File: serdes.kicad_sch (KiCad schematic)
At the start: 11 parts, among them U1 LFE5U-85F-6BG381C

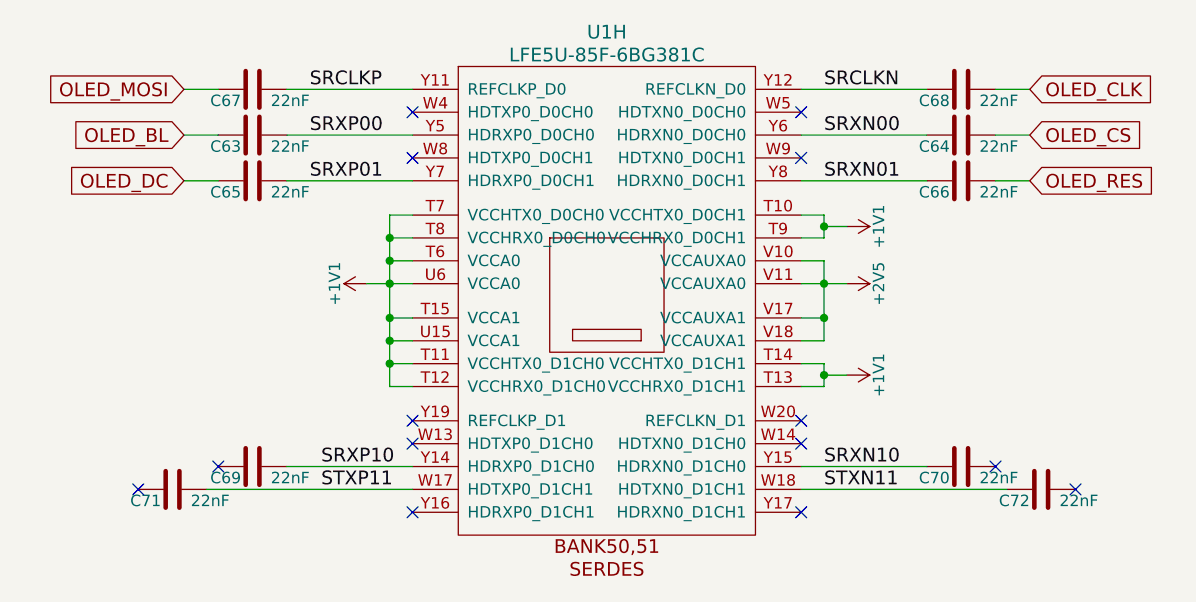
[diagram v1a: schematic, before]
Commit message: remove a few more oled things
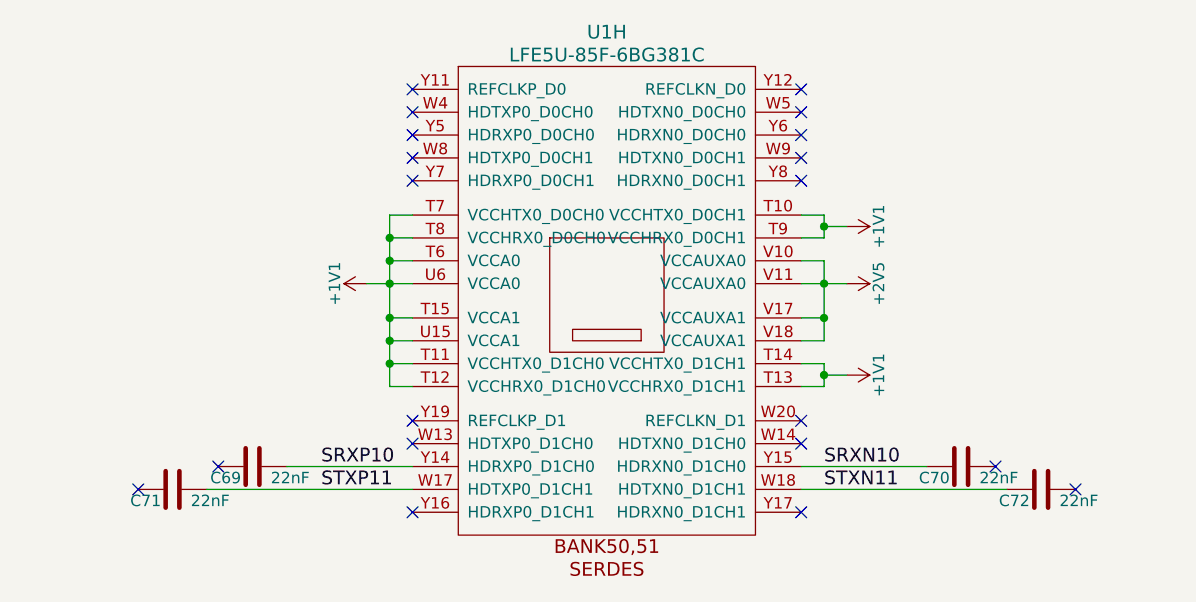
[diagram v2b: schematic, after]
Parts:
- removed C63, C64, C65, C66, C67, C68: 22nF, Capacitor_SMD:C_0603_1608Metric, symbol Device:C
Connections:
- net SRCLKN: no longer names the net of U1.Y12 (REFCLKN_D0)
- net SRCLKP: no longer names the net of U1.Y11 (REFCLKP_D0)
- net SRXN00: no longer names the net of U1.Y6 (HDRXN0_D0CH0)
- net SRXN01: no longer names the net of U1.Y8 (HDRXN0_D0CH1)
- net SRXP00: no longer names the net of U1.Y5 (HDRXP0_D0CH0)
- net SRXP01: no longer names the net of U1.Y7 (HDRXP0_D0CH1)
- no-connect marks 14 -> 20

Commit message: start to normalize bom
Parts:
- C69, C70, C71, C72: Digikey (none) -> 587-1238-1-ND; LCSC (none) -> C107137; MPN (none) -> CX0603MRX7R8BB223
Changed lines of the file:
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@@
+			)
+		)
+		(property "LCSC" "C107137"
+			(at 184.15 91.44 90)
+			(effects
+				(font
+					(size 1.27 1.27)
+				)
+				(hide yes)
+			)
+		)
+		(property "Digikey" "587-1238-1-ND"
+			(at 184.15 91.44 90)
+			(effects
+				(font
+					(size 1.27 1.27)
+				)
+				(hide yes)
+			)
+		)
+		(property "MPN" "CX0603MRX7R8BB223"
+			(at 184.15 91.44 90)
+			(effects
+				(font
+					(size 1.27 1.27)
+				)
+				(hide yes)
 			)
 		)
@@
 			)
 		)
+		(property "LCSC" "C107137"
+			(at 105.41 91.44 90)
+			(effects
+				(font
+					(size 1.27 1.27)
+				)
+				(hide yes)
+			)
+		)
+		(property "Digikey" "587-1238-1-ND"
+			(at 105.41 91.44 90)
+			(effects
+				(font
+					(size 1.27 1.27)
+				)
+				(hide yes)
+			)
+		)
+		(property "MPN" "CX0603MRX7R8BB223"
+			(at 105.41 91.44 90)
+			(effects
+				(font
+					(size 1.27 1.27)
+				)
+				(hide yes)
+			)
+		)
 		(pin "1"
 		)
@@
 			)
 		)
+		(property "LCSC" "C107137"
+			(at 96.52 93.98 90)
+			(effects
+				(font
+					(size 1.27 1.27)
+				)
+				(hide yes)
+			)
+		)
+		(property "Digikey" "587-1238-1-ND"
+			(at 96.52 93.98 90)
+			(effects
+				(font
+					(size 1.27 1.27)
+				)
+				(hide yes)
+			)
+		)
+		(property "MPN" "CX0603MRX7R8BB223"
+			(at 96.52 93.98 90)
+			(effects
+				(font
+					(size 1.27 1.27)
+				)
+				(hide yes)
+			)
+		)
 		(pin "1"
 		)
@@
 			)
 		)
+		(property "LCSC" "C107137"
+			(at 193.04 93.98 90)
+			(effects
+				(font
+					(size 1.27 1.27)
+				)
+				(hide yes)
+			)
+		)
+		(property "Digikey" "587-1238-1-ND"
+			(at 193.04 93.98 90)
+			(effects
+				(font
+					(size 1.27 1.27)
+				)
+				(hide yes)
+			)
+		)
+		(property "MPN" "CX0603MRX7R8BB223"
+			(at 193.04 93.98 90)
+			(effects
+				(font
+					(size 1.27 1.27)
+				)
+				(hide yes)
+			)
+		)

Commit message: updating part numbers across schematcs
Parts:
- C69, C70, C71, C72: MPN CX0603MRX7R8BB223 -> CC0603JRX7R8BB223
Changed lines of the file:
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@@
 			)
 		)
-		(property "MPN" "CX0603MRX7R8BB223"
+		(property "MPN" "CC0603JRX7R8BB223"
 			(at 184.15 91.44 90)
 			(effects
@@
 			)
 		)
-		(property "MPN" "CX0603MRX7R8BB223"
+		(property "MPN" "CC0603JRX7R8BB223"
 			(at 105.41 91.44 90)
 			(effects
@@
 			)
 		)
-		(property "MPN" "CX0603MRX7R8BB223"
+		(property "MPN" "CC0603JRX7R8BB223"
 			(at 96.52 93.98 90)
 			(effects
@@
 			)
 		)
-		(property "MPN" "CX0603MRX7R8BB223"
+		(property "MPN" "CC0603JRX7R8BB223"
 			(at 193.04 93.98 90)
 			(effects

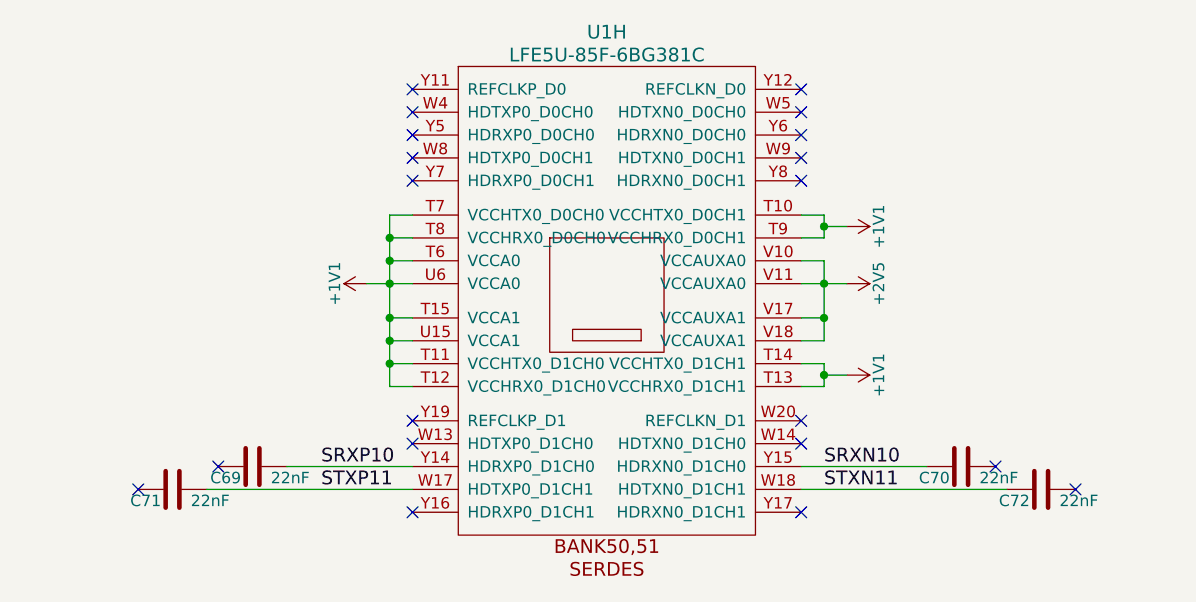
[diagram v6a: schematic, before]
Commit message: remove serdes. fix led connectivity issues
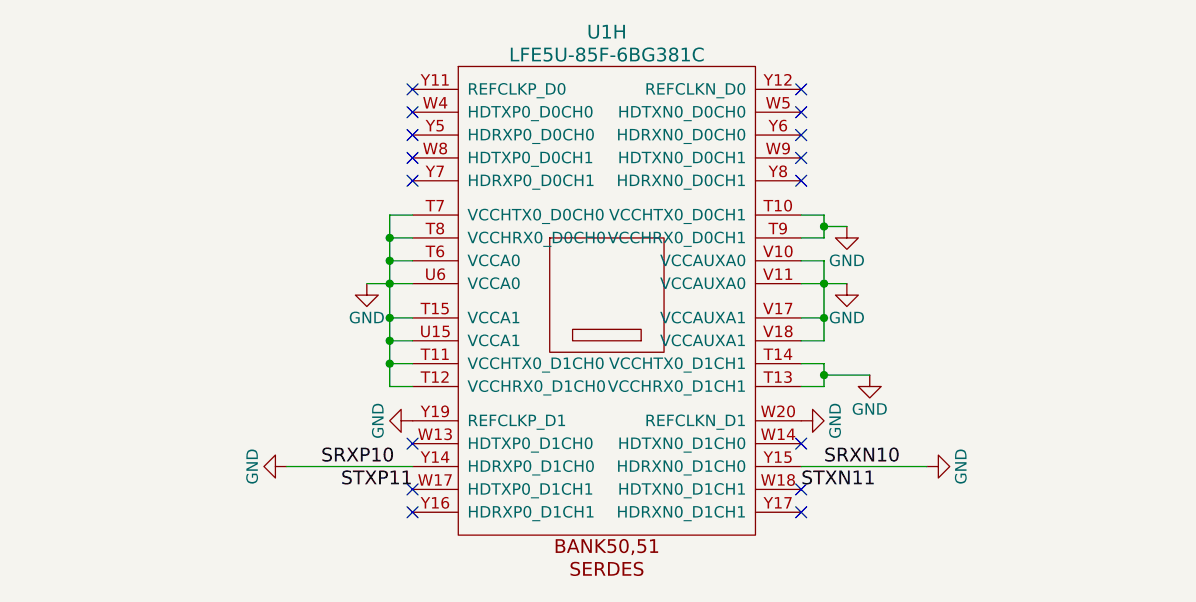
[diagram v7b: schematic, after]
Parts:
- removed C69, C70, C71, C72: 22nF, Capacitor_SMD:C_0603_1608Metric, symbol Device:C
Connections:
- net +1V1 is gone; now on net GND: U1.T10 (VCCHTX0_D0CH1), U1.T11 (VCCHTX0_D1CH0), U1.T12 (VCCHRX0_D1CH0), U1.T13 (VCCHRX0_D1CH1), U1.T14 (VCCHTX0_D1CH1), U1.T15 (VCCA1), U1.T6 (VCCA0), U1.T7 (VCCHTX0_D0CH0), U1.T8 (VCCHRX0_D0CH0), U1.T9 (VCCHRX0_D0CH1), U1.U15 (VCCA1), U1.U6 (VCCA0)
- net +2V5 is gone; now on net GND: U1.V10 (VCCAUXA0), U1.V11 (VCCAUXA0), U1.V17 (VCCAUXA1), U1.V18 (VCCAUXA1)
- net SRXN10 is gone; now on net GND: U1.Y15 (HDRXN0_D1CH0)
- net SRXP10 is gone; now on net GND: U1.Y14 (HDRXP0_D1CH0)
- net GND: now reaches U1.W20 (REFCLKN_D1)
- net GND: now also U1.Y19 (REFCLKP_D1)
- no-connect marks 20 -> 16
